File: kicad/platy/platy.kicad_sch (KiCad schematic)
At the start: 85 parts, among them J1 Conn_01x04_Socket, J2 Conn_01x02_Socket, J3 Conn_Coaxial, J5 USB_C_Receptacle_USB2.0_16P, J6 Conn_01x05_Pin, J8 Conn_01x14_Socket, J9 Conn_02x04_Odd_Even, Q4 BC847, Q5 Q_PMOS_GSD, SW2 SW_Push(Boot), SW3 SW_Push(EN), U10 ESP32-S3-WROOM-1, U4 CC1101, U5 PN5321A3HN_C1xx, U6 TSOP382xx, U7 AMS1117-3.3, Y2 27.12Mhz, Y3 26MHz

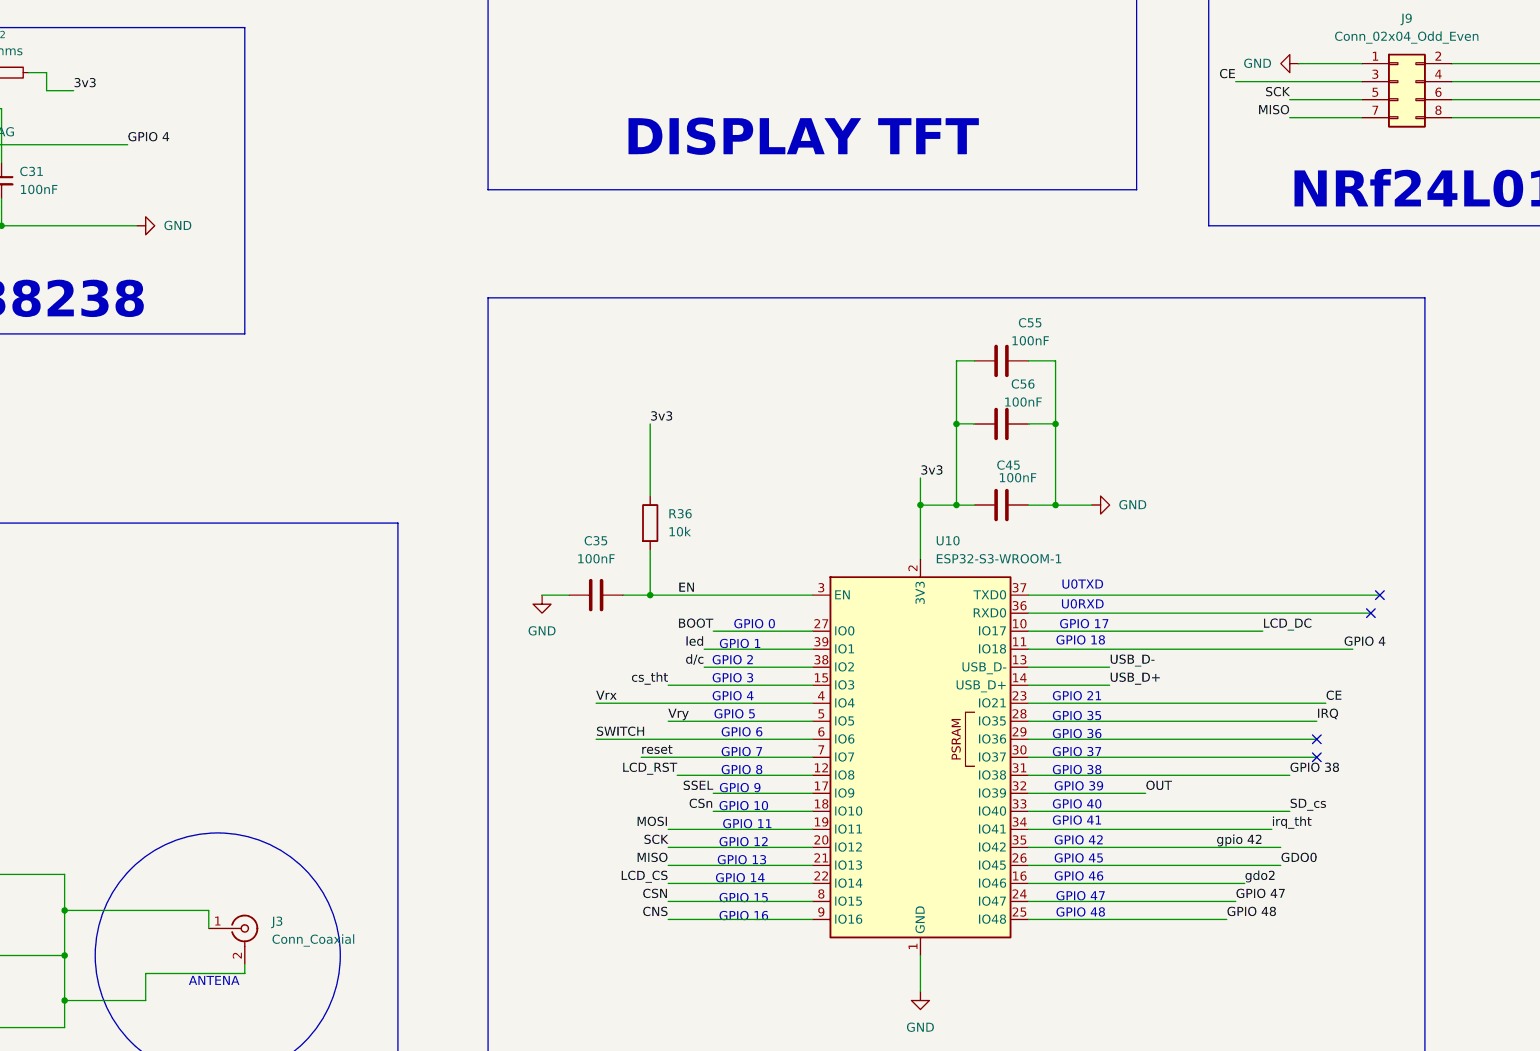
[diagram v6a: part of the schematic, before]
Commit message: changes the naming mismatched and the some pin connnection also
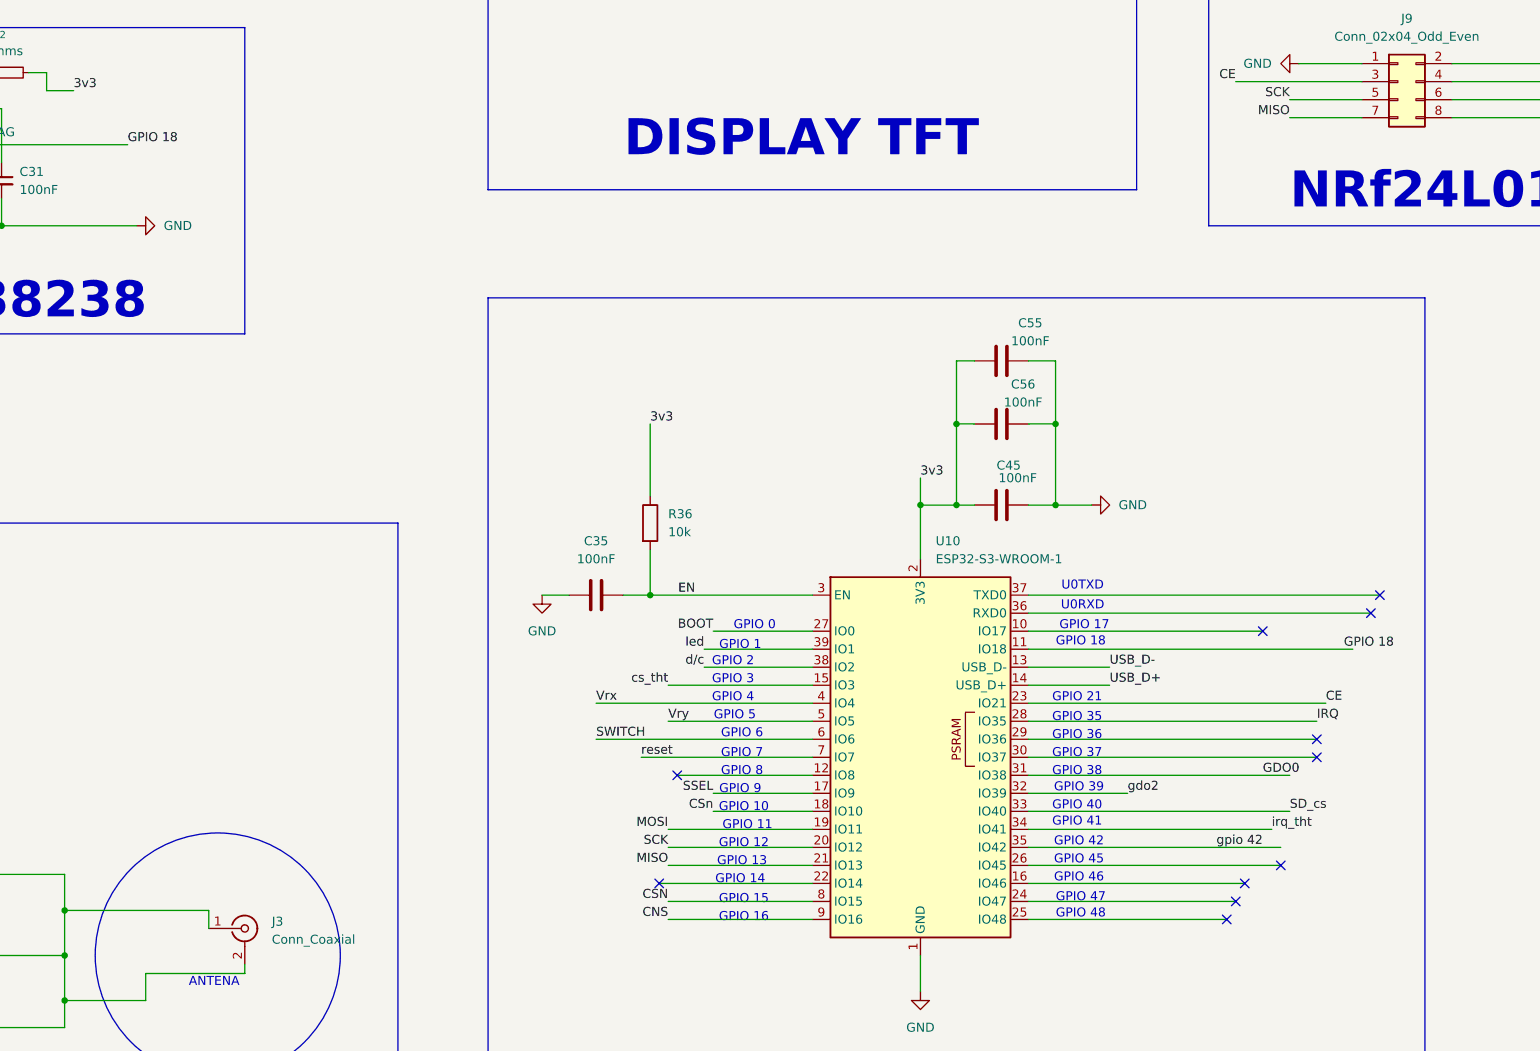
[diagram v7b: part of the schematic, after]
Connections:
- net GPIO 38 is gone; now on net GDO0: U10.31 (IO38)
- net OUT is gone; now on net gdo2: U10.32 (IO39)
- net GDO0: no longer U10.26 (IO45)
- net gdo2: no longer U10.16 (IO46)
- net GPIO 4 renamed GPIO 18
- net GPIO 47: no longer names the net of U10.24 (IO47)
- net GPIO 48: no longer names the net of U10.25 (IO48)
- net LCD_CS: no longer names the net of U10.22 (IO14)
- net LCD_DC: no longer names the net of U10.10 (IO17)
- net LCD_RST: no longer names the net of U10.12 (IO8)
- no-connect marks 12 -> 19
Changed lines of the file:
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@@
 	)
 	(no_connect
+		(at 378.46 201.93)
+	)
+	(no_connect
 		(at 308.61 340.36)
 	)
 	(no_connect
+		(at 377.19 204.47)
+	)
+	(no_connect
+		(at 382.27 163.83)
+	)
+	(no_connect
+		(at 299.72 184.15)
+	)
+	(no_connect
 		(at 397.51 161.29)
 	)
@@
 	)
 	(no_connect
+		(at 379.73 199.39)
+	)
+	(no_connect
 		(at 151.13 245.11)
 	)
@@
 	)
 	(no_connect
+		(at 297.18 199.39)
+	)
+	(no_connect
 		(at 99.06 242.57)
 	)
@@
 		(at 308.61 342.9)
 	)
+	(no_connect
+		(at 384.81 196.85)
+	)
 	(wire
 		(pts
@@
 	(wire
 		(pts
-			(xy 298.45 199.39) (xy 318.77 199.39)
-		)
-		(stroke
-			(width 0)
-			(type default)
-		)
-	)
-	(wire
-		(pts
 			(xy 210.82 85.09) (xy 210.82 87.63)
 		)
@@
 	(wire
 		(pts
+			(xy 349.25 186.69) (xy 363.22 186.69)
+		)
+		(stroke
+			(width 0)
+			(type default)
+		)
+	)
+	(wire
+		(pts
 			(xy 147.32 212.09) (xy 147.32 213.36)
 		)
@@
 	(wire
 		(pts
-			(xy 349.25 186.69) (xy 365.76 186.69)
-		)
-		(stroke
-			(width 0)
-			(type default)
-		)
-	)
-	(wire
-		(pts
 			(xy 92.71 257.81) (xy 92.71 261.62)
 		)
@@
 	(wire
 		(pts
+			(xy 297.18 199.39) (xy 318.77 199.39)
+		)
+		(stroke
+			(width 0)
+			(type default)
+		)
+	)
+	(wire
+		(pts
 			(xy 349.25 166.37) (xy 394.97 166.37)
 		)
@@
 		)
 	)
+	(label "gdo2"
+		(at 363.22 186.69 0)
+		(effects
+			(font
+				(size 1.27 1.27)
+			)
+			(justify left bottom)
+		)
+	)
 	(label "RSTPD_N"
 		(at 88.9 209.55 0)
@@
 		)
 	)
-	(label "LCD_CS"
-		(at 298.45 199.39 180)
-		(effects
-			(font
-				(size 1.27 1.27)
-			)
-			(justify right bottom)
-		)
-	)
 	(label "irq_tht"
 		(at 297.18 71.12 180)
@@
 		)
 	)
-	(label "LCD_DC"
-		(at 382.27 163.83 0)
-		(effects
-			(font
-				(size 1.27 1.27)
-			)
-			(justify left bottom)
-		)
-	)
 	(label "INT0"
 		(at 91.44 237.49 0)
@@
 		)
 	)
-	(label "gdo2"
-		(at 379.73 199.39 0)
-		(effects
-			(font
-				(size 1.27 1.27)
-			)
-			(justify left bottom)
-		)
-	)
-	(label "GDO0"
-		(at 384.81 196.85 0)
-		(effects
-			(font
-				(size 1.27 1.27)
-			)
-			(justify left bottom)
-		)
-	)
 	(label "Vrx"
 		(at 400.05 48.26 0)
@@
 		)
 	)
-	(label "GPIO 4"
+	(label "GPIO 18"
 		(at 393.7 166.37 0)
 		(effects
@@
 		)
 	)
-	(label "OUT"
-		(at 365.76 186.69 0)
-		(effects
-			(font
-				(size 1.27 1.27)
-			)
-			(justify left bottom)
-		)
-	)
 	(label "SSEL{slash}SCL{slash}RX"
 		(at 218.44 297.18 0)
@@
 		)
 	)
-	(label "GPIO 48"
-		(at 377.19 204.47 0)
-		(effects
-			(font
-				(size 1.27 1.27)
-			)
-			(justify left bottom)
-		)
-	)
 	(label "reset"
 		(at 297.18 45.72 180)
@@
 		)
 	)
-	(label "GPIO 4"
+	(label "GPIO 18"
 		(at 222.25 95.25 0)
 		(effects
@@
 		)
 	)
-	(label "GPIO 38"
-		(at 386.08 184.15 0)
-		(effects
-			(font
-				(size 1.27 1.27)
-			)
-			(justify left bottom)
-		)
-	)
 	(label "3v3"
 		(at 214.63 87.63 0)
@@
 		)
 	)
-	(label "GPIO 47"
-		(at 378.46 201.93 0)
-		(effects
-			(font
-				(size 1.27 1.27)
-			)
-			(justify left bottom)
-		)
-	)
 	(label "SSEL"
 		(at 304.8 186.69 180)
@@
 		)
 	)
-	(label "LCD_RST"
-		(at 299.72 184.15 180)
-		(effects
-			(font
-				(size 1.27 1.27)
-			)
-			(justify right bottom)
-		)
-	)
 	(label "SWITCH"
 		(at 288.29 179.07 0)
@@
 		)
 	)
+	(label "GDO0"
+		(at 382.27 184.15 0)
+		(effects
+			(font
+				(size 1.27 1.27)
+			)
+			(justify left bottom)
+		)
+	)

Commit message: changes made in the impedance of the antenna and the make the circuit of the aligned straight
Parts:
- removed R8, R9: 4.7K, Resistor_SMD:R_0805_2012Metric, symbol Device:R_Small
- added C1, C2, C3, C4: NC, Capacitor_SMD:C_0805_2012Metric, symbol Device:C_Small
- added R1, R2: 1.5, Resistor_SMD:R_0805_2012Metric, symbol Device:R
- added R3, R4: NC, Resistor_SMD:R_0805_2012Metric, symbol Device:R_Small
- J3: footprint Connector_Coaxial:U.FL_Molex_MCRF_73412-0110_Vertical -> Connector_Coaxial:U.FL_Hirose_U.FL-R-SMT-1_Vertical
- R14: value R -> 56k
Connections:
- net GND: now also C3.1, C4.2, R3.1, R4.2; no longer C27.2, C28.2, C29.2, C30.1, D3.2 (A), J3.1 (In), J3.2 (Ext)
- net at C26.2, C28.1, L4.2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: now also C2.1
- net at C25.1, C27.1, L3.2: now also C1.1
- net at Q5.1 (G), R37.1: now also D3.2 (A)
- new net: C1.2, C27.2, C29.2, C3.2, R1.1
- new net: J3.1 (In), R1.2, R4.1
- new net: J3.2 (Ext), R2.1, R3.2
- new net: C2.2, C28.2, C30.1, C4.1, R2.2
